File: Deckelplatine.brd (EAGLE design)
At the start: 110 x 75 mm, 62 parts, among them IC1 MAX1487EESA+, IC2 74HCT595D, IC3 74HCT595D, IC4 74HCT595D, IC5 74HCT595D, IC6 74HCT595D, J1 52808-2570, U1 LM2676S, X1 236-406/000-023, X2 233-502

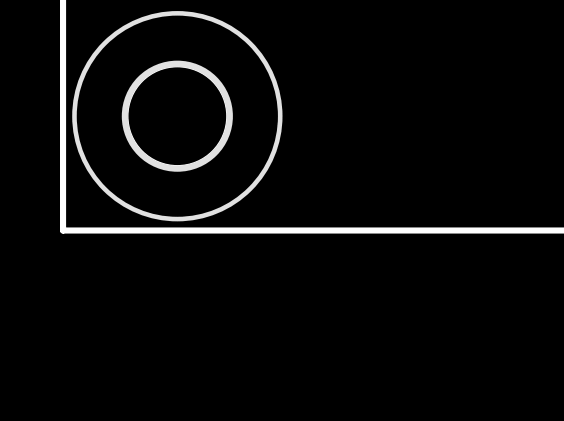
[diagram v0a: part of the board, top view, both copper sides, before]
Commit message: Shift Register Pullup Widerstände eingefügt
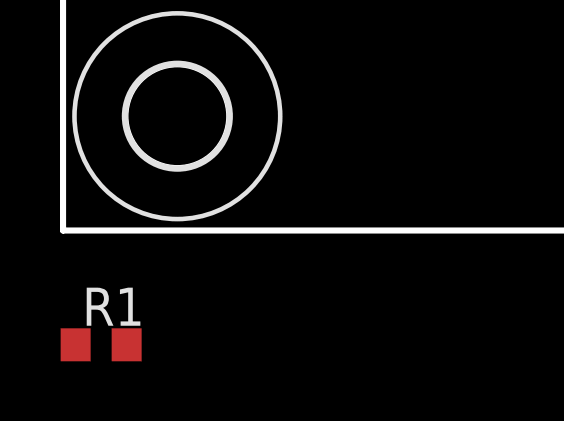
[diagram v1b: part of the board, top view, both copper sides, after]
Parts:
- added R1: 10k, RA-GAS Projekte LTD:R0603

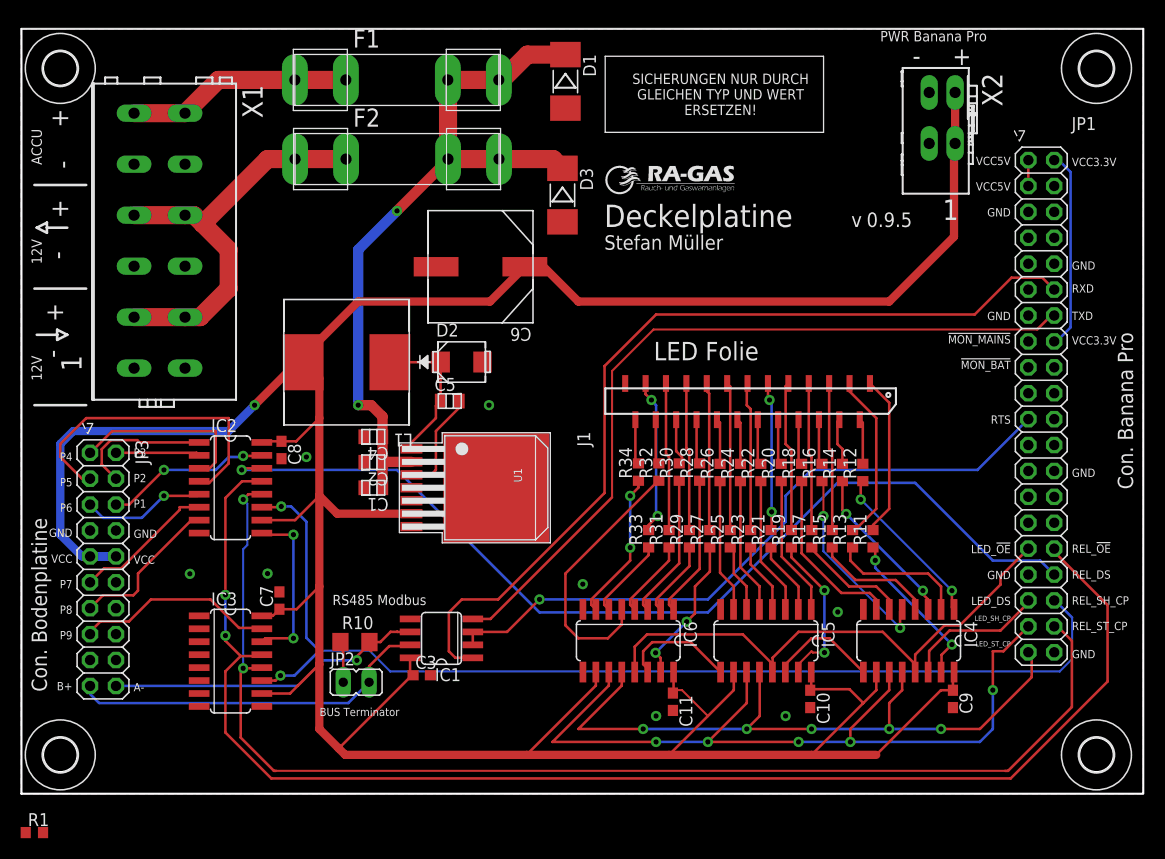
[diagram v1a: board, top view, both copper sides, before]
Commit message: Realis Shift Register verschoben
Die Schiebe Register für die Relais waren dem Stecker für die Verbindung zur Bodenplatine im Weg.
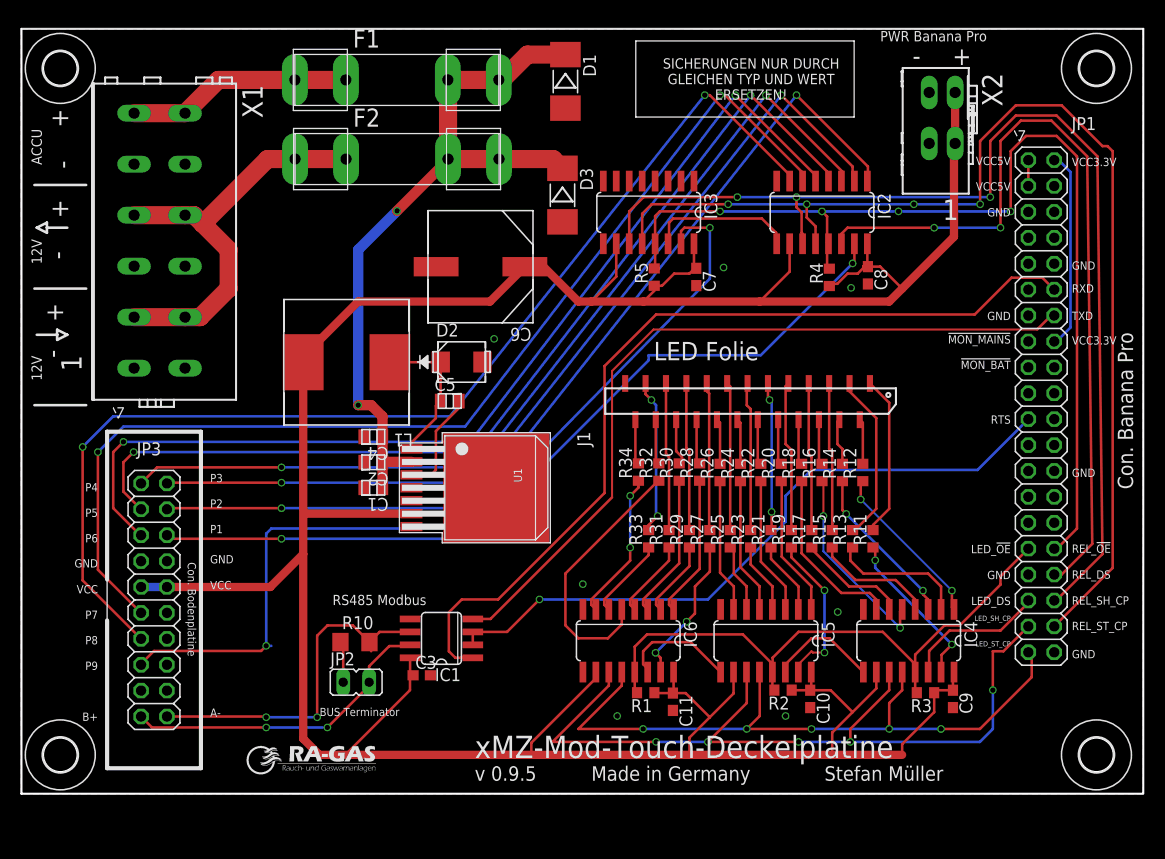
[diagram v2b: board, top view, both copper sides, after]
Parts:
- removed U$3: (no value), xMZ-Mod-Touch-Bodenplatine:TEXT_NAME_VERSION_AUTHOR-SMALL
- added R2, R3, R4, R5: 10k, RA-GAS Projekte LTD:R0603
- added U$5: (no value), xMZ-Mod-Touch-Bodenplatine:A3-LOC-RA-GAS
- added U$6: (no value), xMZ-Mod-Touch-Bodenplatine:TEXT_NAME_VERSION_AUTHOR-SMALL
- JP1: value '' -> (none)
- moved U$2 66.9 mm to (22.1, 1.91)
- moved IC2 64.0 mm to (78.5, 57.0), turned to 180 degrees
- moved R1 61.5 mm to (61.2, 9.91), turned to 180 degrees
- moved IC3 60.1 mm to (61.5, 57.0), turned to 180 degrees
- moved C8 60.0 mm to (83.0, 50.8)
- moved C7 51.7 mm to (66.2, 50.7), turned to 270 degrees
- moved JP3 5.83 mm to (13.0, 19.0)
- moved U$4 3.35 mm to (71.6, 70.1)
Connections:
- net LED_!OE: now also R1.2, R2.2, R3.2
- net REL_!OE: now also R4.2, R5.2
- net VCC: now also R1.1, R2.1, R3.1, R4.1, R5.1
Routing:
- net P8: track 15.3 -> 111.0 mm, vias 0 -> 2
- net P7: track 13.9 -> 107.6 mm, vias 0 -> 2
- net P6: track 12.2 -> 99.2 mm, vias 1 -> 2
- net P3: track 8.26 -> 90.1 mm, vias 0 -> 2
- net P2: track 13.5 -> 92.7 mm, vias 0 -> 2
- net P4: track 18.3 -> 91.3 mm, vias 0 -> 2
- net P9: track 19.6 -> 87.8 mm, vias 0 -> 2
- net P5: track 30.8 -> 96.0 mm, vias 0 -> 2
- net P1: track 16.3 -> 80.9 mm
- net REL_!OE: track 138.1 -> 99.7 mm, vias 2 -> 4
- net REL_DS: track 96.5 -> 79.1 mm, vias 1 -> 2
- net VCC: track 331.0 -> 318.7 mm, vias 1 -> 0
- net REL_ST_CP: track 121.9 -> 112.2 mm, vias 2 -> 4
- net LED_!OE: track 53.8 -> 59.9 mm
- net B+: track 35.8 -> 31.3 mm, vias 0 -> 2
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
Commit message: BAT und MAINS Monitor
Konnectoren in eigener Bibliothek 'Deckelplatine.lbr'
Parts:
- removed U$2: (no value), xMZ-Mod-Touch-Bodenplatine:LOGO_RA-GAS-SMALL
- removed U$4: (no value), xMZ-Mod-Touch-Bodenplatine:TEXT_FUSE-SMALL
- added D4: LL4005G, diode:MELF-MLL41
- added D5, D6: (no value), Deckelplatine:SOD523
- added R6, R7: 2.7k, RA-GAS Projekte LTD:R0603
- added R8, R9: 1k, RA-GAS Projekte LTD:R0603
- added U$3: (no value), Deckelplatine:TEXT_NAME_VERSION_AUTHOR-SMALL
- U$6: device xMZ-Mod-Touch-Bodenplatine:TEXT_NAME_VERSION_AUTHOR-SMALL -> Deckelplatine:LOGO_RA-GAS-SMALL
- moved D3 170.7 mm to (186.7, 164.8), turned to 90 degrees
- moved D1 167.0 mm to (193.0, 161.3), turned to 90 degrees
- moved C9 165.2 mm to (227.2, 103.3)
- moved D2 165.2 mm to (179.1, 136.3)
- moved H3 165.2 mm to (241.3, 165.1)
- moved H4 165.2 mm to (241.3, 97.8)
- moved L1 165.2 mm to (167.8, 136.3)
- moved R1 165.2 mm to (197.1, 103.9)
- moved R10 165.2 mm to (168.6, 108.8)
- moved R4 165.2 mm to (215.1, 144.6)
- moved C1 165.2 mm to (170.4, 124.0)
- moved C11 165.2 mm to (199.8, 103.0)
- moved C2 165.2 mm to (170.4, 126.5)
- moved C3 165.2 mm to (175.1, 105.6)
- moved C6 165.2 mm to (180.9, 145.7)
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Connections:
- removed net !MON_BAT: JP1.17
- removed net !MON_MAINS: JP1.15
- new net MON_BAT: D6.C, JP1.17, R7.1, R9.2
- new net MON_MAINS: D5.C, JP1.15, R6.1, R8.2
- new net N$37: D1.C, D4.A, F2.2A, F2.2B, R6.2
- net GND: now also D5.A, D6.A, R8.1, R9.1
- net N$4: now also D4.C, R7.2; no longer D1.C, F2.2A, F2.2B
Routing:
- net MON_BAT: track 0.00 -> 87.7 mm, vias 0 -> 1
- net MON_MAINS: track 0.00 -> 77.0 mm, vias 0 -> 1
- net N$37: track 0.00 -> 21.8 mm
- net N$4: track 72.4 -> 67.5 mm
- net P2: track 92.7 -> 89.9 mm
- net P4: track 91.3 -> 88.6 mm
- net P3: track 90.1 -> 87.4 mm
- net P5: track 96.0 -> 93.5 mm
- net P6: track 99.2 -> 97.4 mm
- net REL_DS: track 79.1 -> 77.4 mm
- net REL_ST_CP: track 112.2 -> 110.6 mm
- net REL_SH_CP: track 108.4 -> 107.5 mm
- net A-: track 34.3 -> 33.6 mm
- net P9: track 87.8 -> 87.3 mm
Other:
- board text added: "12V INPUT"
- board text added: "12V OUT"
- board text added: "Connector Banana Pro"
- board text added: "Connector Bodenplatine"
- board text removed: "12V"
- board text removed: "Con. Banana Pro"
- board text removed: "Con. Bodenplatine"

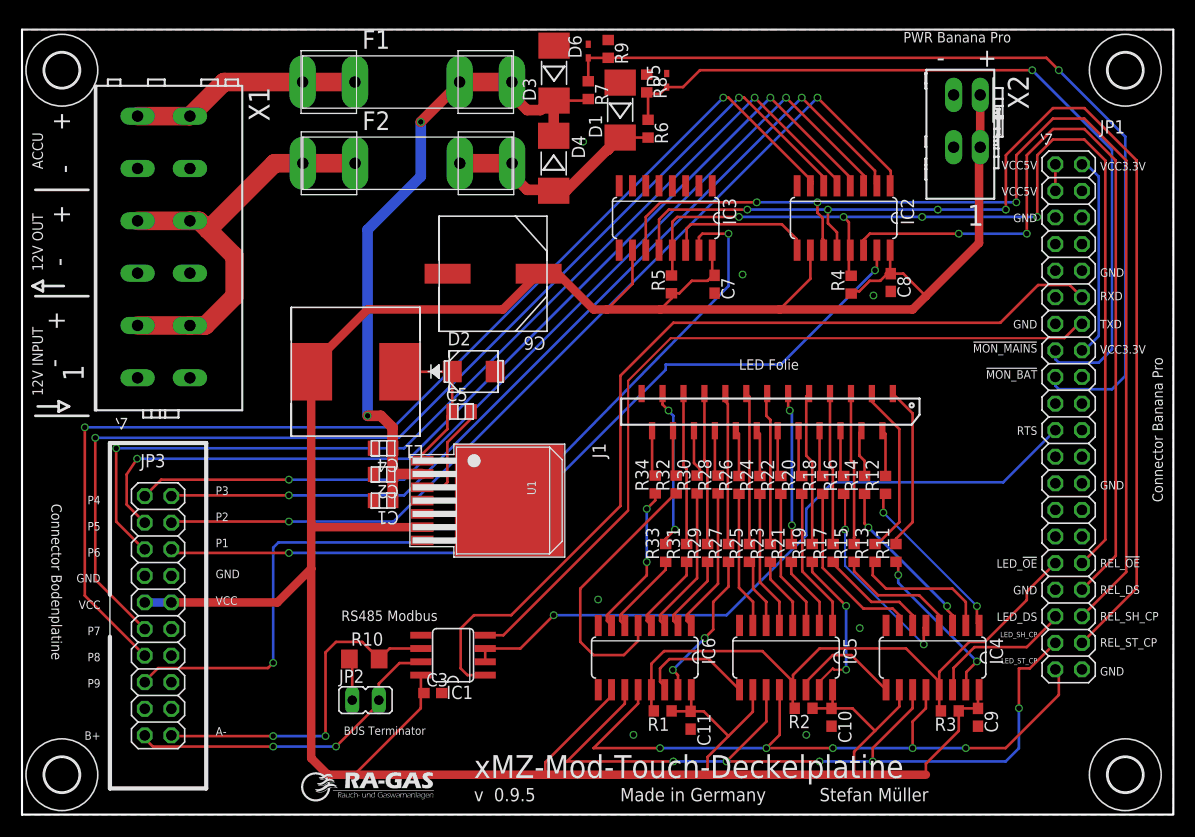
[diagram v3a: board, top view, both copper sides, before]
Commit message: Keine Airwire und DRC ist OK
Sparkfun Design-Rule Check ist noch nicht erfüllt, hauptsächlich Winkel der Leiterbahnen und Abstände zu gering.
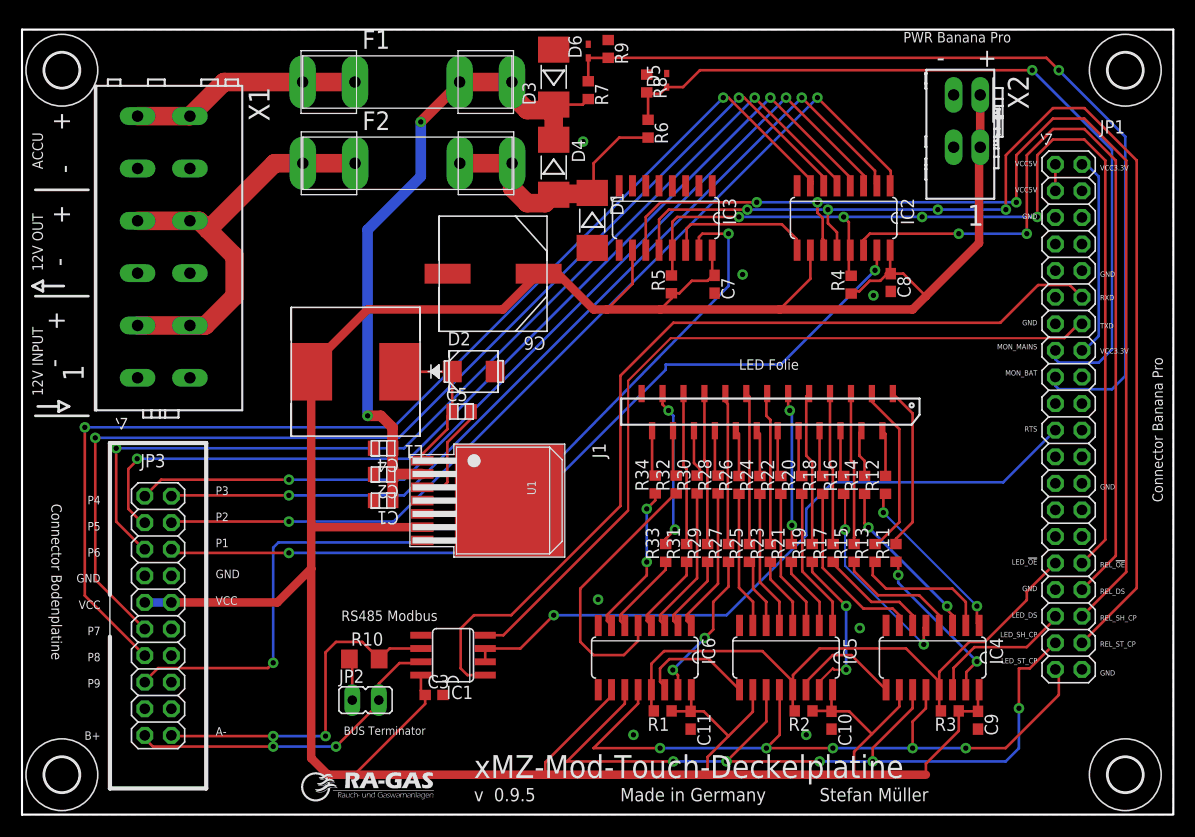
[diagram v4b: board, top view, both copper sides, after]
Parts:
- C3: value 100n -> 0.1uF
- D5, D6: value (none) -> MM5Z3V3
- JP1: value (none) -> CON 2x20
- JP3: value '' -> CON 2x10
- moved D1 10.9 mm to (190.4, 150.7), turned to 270 degrees
- moved D3 0.38 mm to (186.7, 164.4)
- moved D4 0.38 mm to (186.7, 155.8)
- moved C10 0.28 mm to (213.2, 103.0)
- moved C9 0.28 mm to (227.2, 103.0)
- moved R2 0.25 mm to (210.6, 103.9)
- moved C3 0.22 mm to (175.3, 105.4)
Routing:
- net N$37: track 21.8 -> 25.1 mm
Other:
- board text added: "MON_BAT"
- board text added: "MON_MAINS"
- board text removed: "!MON_BAT"
- board text removed: "!MON_MAINS"

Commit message: BOM und kontrolliert und eingfügt
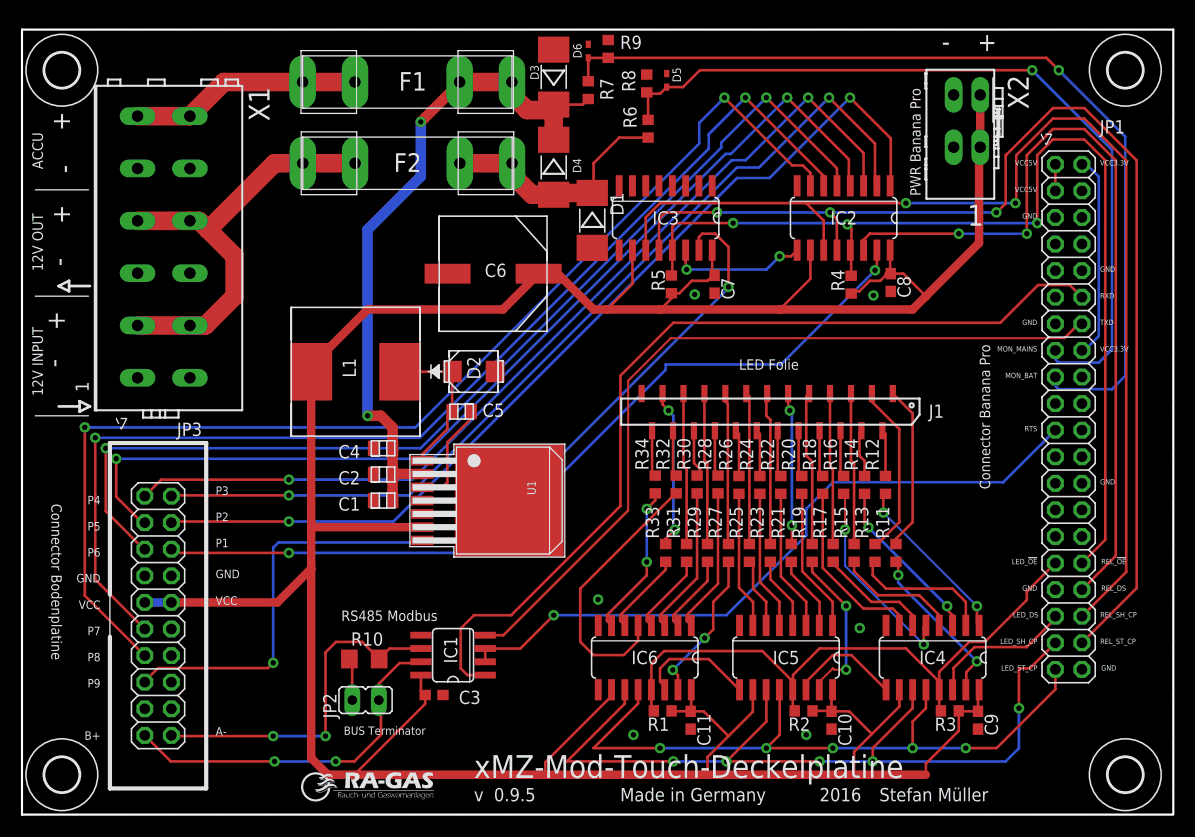
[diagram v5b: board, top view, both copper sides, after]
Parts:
- X1: device con-wago_236:P-236-406 -> Deckelplatine:P-236-406
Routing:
- net P5: track 93.6 -> 96.7 mm
- net B+: track 31.5 -> 34.5 mm
- net P6: track 97.4 -> 99.7 mm
- net P2: track 89.9 -> 91.7 mm
- net P3: track 87.4 -> 88.9 mm
- net P8: track 110.5 -> 111.9 mm
- net N$4: track 67.4 -> 66.0 mm
- net N$37: track 25.1 -> 23.7 mm
- net P4: track 88.6 -> 89.8 mm
- net P7: track 107.3 -> 108.1 mm
- net P9: track 87.3 -> 86.5 mm
- net LED_ST_CP: track 68.7 -> 67.9 mm
- net REL_!OE: track 99.6 -> 98.9 mm, vias 4 -> 3
- net REL_ST_CP: track 110.6 -> 109.9 mm, vias 4 -> 3
- net N$3: track 14.5 -> 13.8 mm, vias 0 -> 2
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
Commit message: Board auf Koordinaten 0x0 ausgerichtet
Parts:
- moved R8 165.2 mm to (59.7, 69.8)
- moved C9 165.2 mm to (91.3, 9.02)
- moved D2 165.2 mm to (43.2, 42.3)
- moved D5 165.2 mm to (61.6, 70.1)
- moved H3 165.2 mm to (105.4, 71.1)
- moved H4 165.2 mm to (105.4, 3.81)
- moved L1 165.2 mm to (31.9, 42.3)
- moved R1 165.2 mm to (61.2, 9.91)
- moved R10 165.2 mm to (32.7, 14.9)
- moved R4 165.2 mm to (79.2, 50.6)
- moved C1 165.2 mm to (34.5, 30.0)
- moved C10 165.2 mm to (77.3, 9.02)
- moved C11 165.2 mm to (63.9, 9.02)
- moved C2 165.2 mm to (34.5, 32.5)
- moved C6 165.2 mm to (45.0, 51.7)
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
